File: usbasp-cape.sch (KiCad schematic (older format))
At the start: 1 part

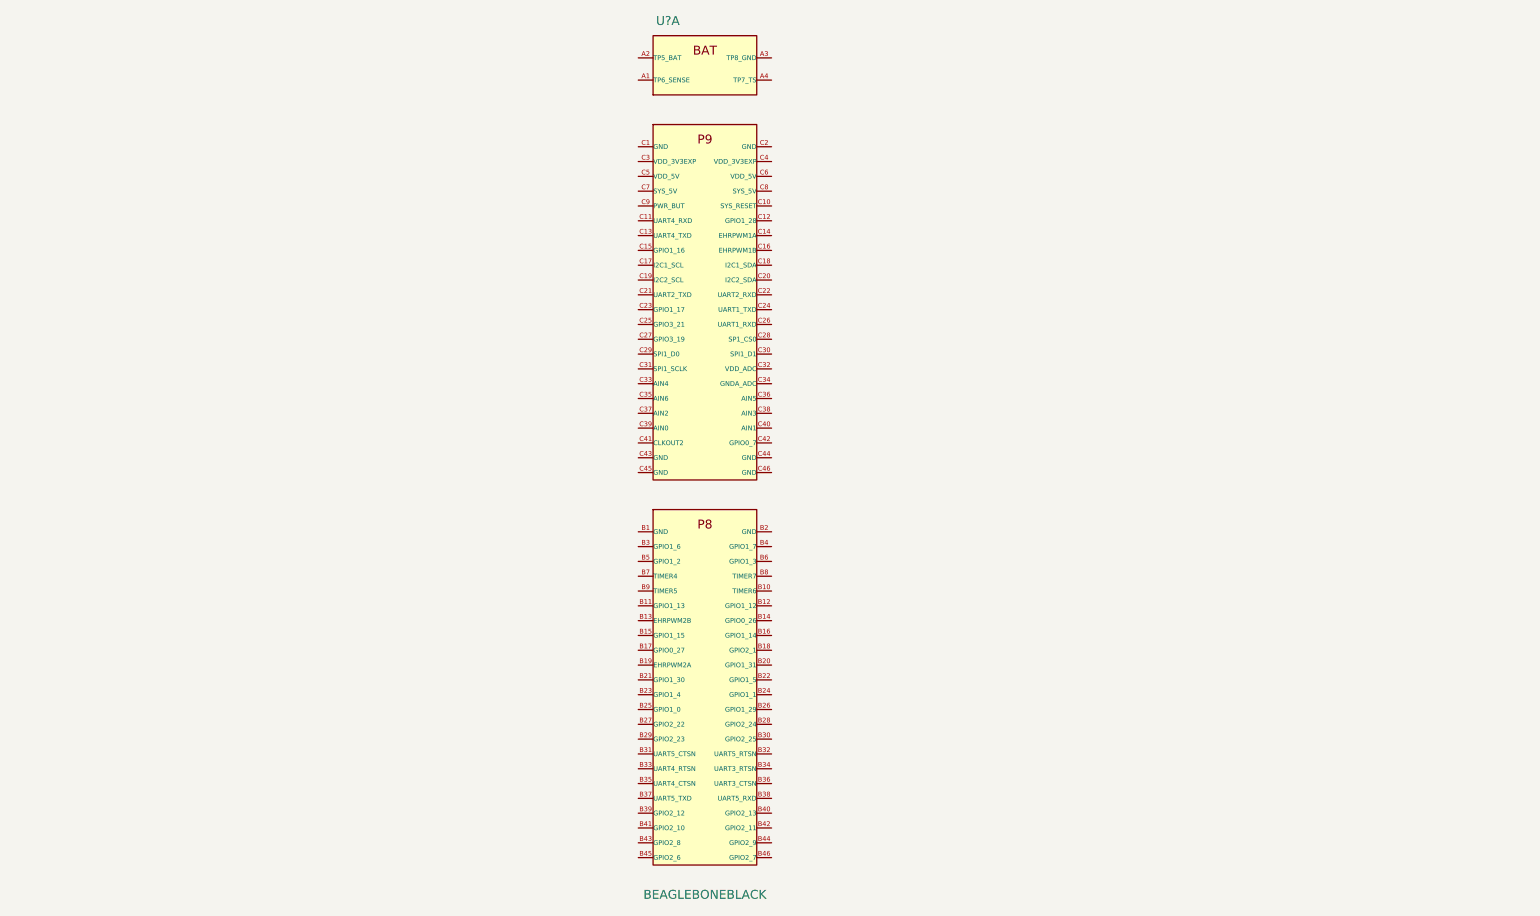
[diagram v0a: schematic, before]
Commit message: add mux and connectors to schematic
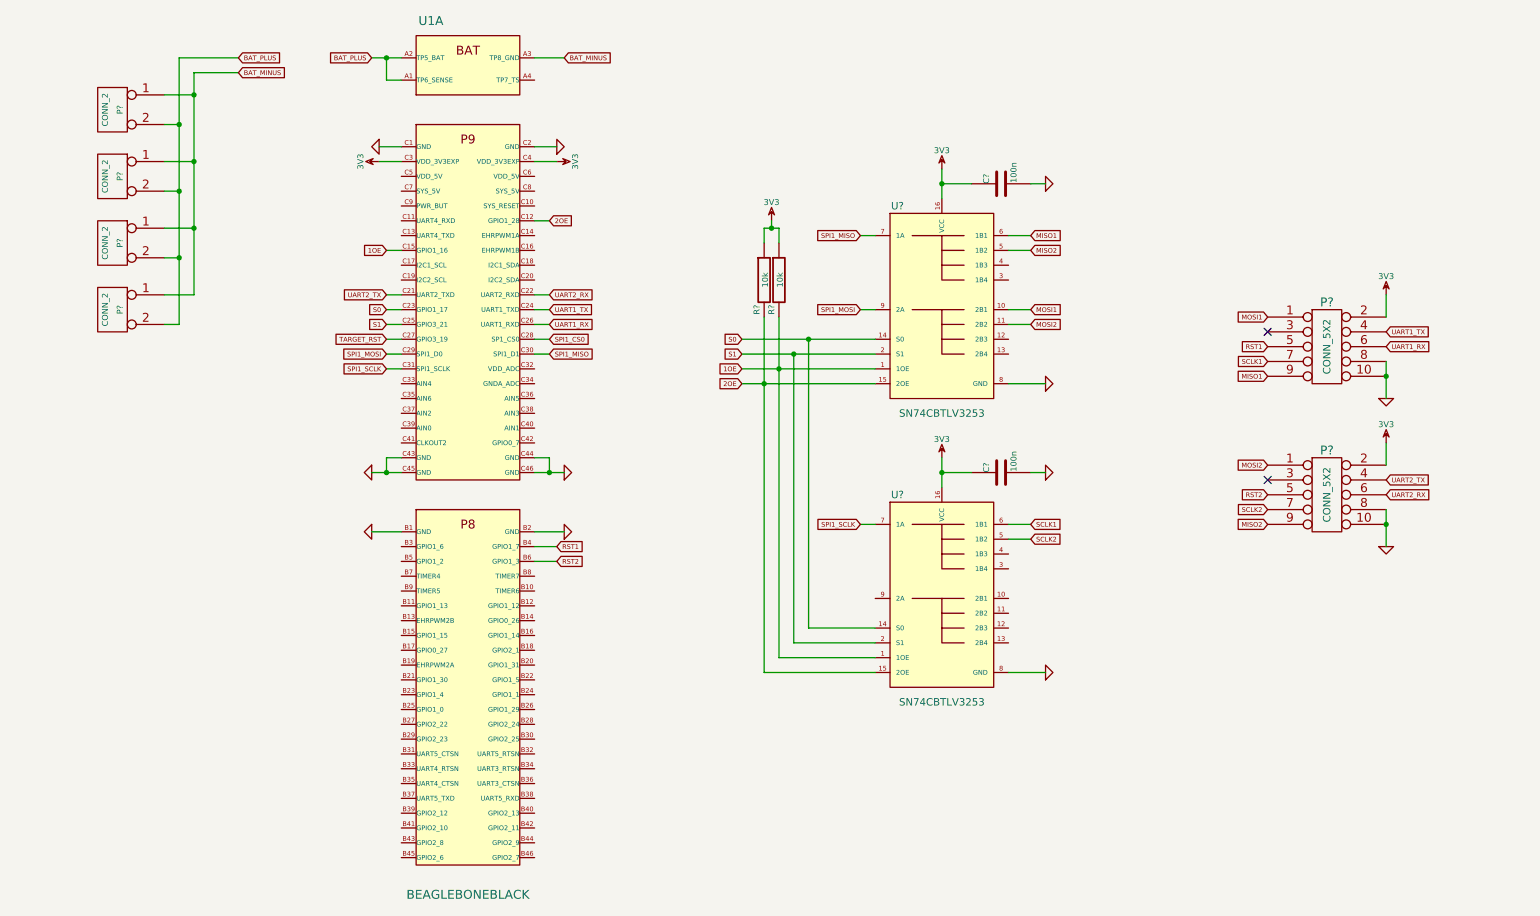
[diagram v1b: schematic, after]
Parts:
- added C? (x2): 100n, symbol C
- added P? (x4): CONN_2, symbol CONN_2
- added P? (x2): CONN_5X2, symbol CONN_5X2
- added R? (x2): 10k, symbol R
- added U? (x2): SN74CBTLV3253, symbol SN74CBTLV3253
- gave numbers to parts that had none: 1
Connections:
- net BAT_PLUS: now reaches U1.A1 (TP6_SENSE)
- net BAT_PLUS: now also U1.A2 (TP5_BAT), P?.2 (PM), P?.2 (PM), P?.2 (PM), P?.2 (PM)
- net BAT_MINUS: now reaches U1.A3 (TP8_GND)
- net BAT_MINUS: now also P?.1 (P1), P?.1 (P1), P?.1 (P1), P?.1 (P1)
- net GND: now reaches U1.B1 (GND)
- net GND: now also U1.B2 (GND), U1.C1 (GND), U1.C2 (GND), U1.C43 (GND), U1.C44 (GND), U1.C45 (GND), U1.C46 (GND), C?.2, C?.2, P?.10, P?.10, P?.8, P?.8, U?.8 (GND), U?.8 (GND)
- net RST1: now reaches U1.B4 (GPIO1_7)
- net RST1: now also P?.5
- net RST2: now reaches U1.B6 (GPIO1_3)
- net RST2: now also P?.5
- net 2OE: now reaches U1.C12 (GPIO1_28)
- net 2OE: now also R?.2, U?.15 (2OE), U?.15 (2OE)
- net 1OE: now reaches U1.C15 (GPIO1_16)
- net 1OE: now also R?.2, U?.1 (1OE), U?.1 (1OE)
- net UART2_TX: now reaches U1.C21 (UART2_TXD)
- net UART2_TX: now also P?.4
- net UART2_RX: now reaches U1.C22 (UART2_RXD)
- net UART2_RX: now also P?.6
- net S0: now reaches U1.C23 (GPIO1_17)
- net S0: now also U?.14 (S0), U?.14 (S0)
- net UART1_TX: now reaches U1.C24 (UART1_TXD)
- net UART1_TX: now also P?.4
- net S1: now reaches U1.C25 (GPIO3_21)
- net S1: now also U?.2 (S1), U?.2 (S1)
- net UART1_RX: now reaches U1.C26 (UART1_RXD)
- net UART1_RX: now also P?.6
- net TARGET_RST: now reaches U1.C27 (GPIO3_19)
- net SPI1_CS0: now reaches U1.C28 (SP1_CS0)
- net SPI1_MOSI: now reaches U1.C29 (SPI1_D0)
- net SPI1_MOSI: now also U?.9 (2A)
- net 3V3: now reaches U1.C3 (VDD_3V3EXP)
- net 3V3: now also U1.C4 (VDD_3V3EXP), C?.1, C?.1, P?.2, P?.2, R?.1, R?.1, U?.16 (VCC), U?.16 (VCC)
- net SPI1_MISO: now reaches U1.C30 (SPI1_D1)
- net SPI1_MISO: now also U?.7 (1A)
- net SPI1_SCLK: now reaches U1.C31 (SPI1_SCLK)
- net SPI1_SCLK: now also U?.7 (1A)
- new net MISO1: P?.9, U?.6 (1B1)
- new net MISO2: P?.9, U?.5 (1B2)
- new net MOSI1: P?.1, U?.10 (2B1)
- new net MOSI2: P?.1, U?.11 (2B2)
- new net SCLK1: P?.7, U?.6 (1B1)
- new net SCLK2: P?.7, U?.5 (1B2)
- no-connect marks 0 -> 2
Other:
- moved on the sheet: U1A

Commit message: add INA219 to schematic
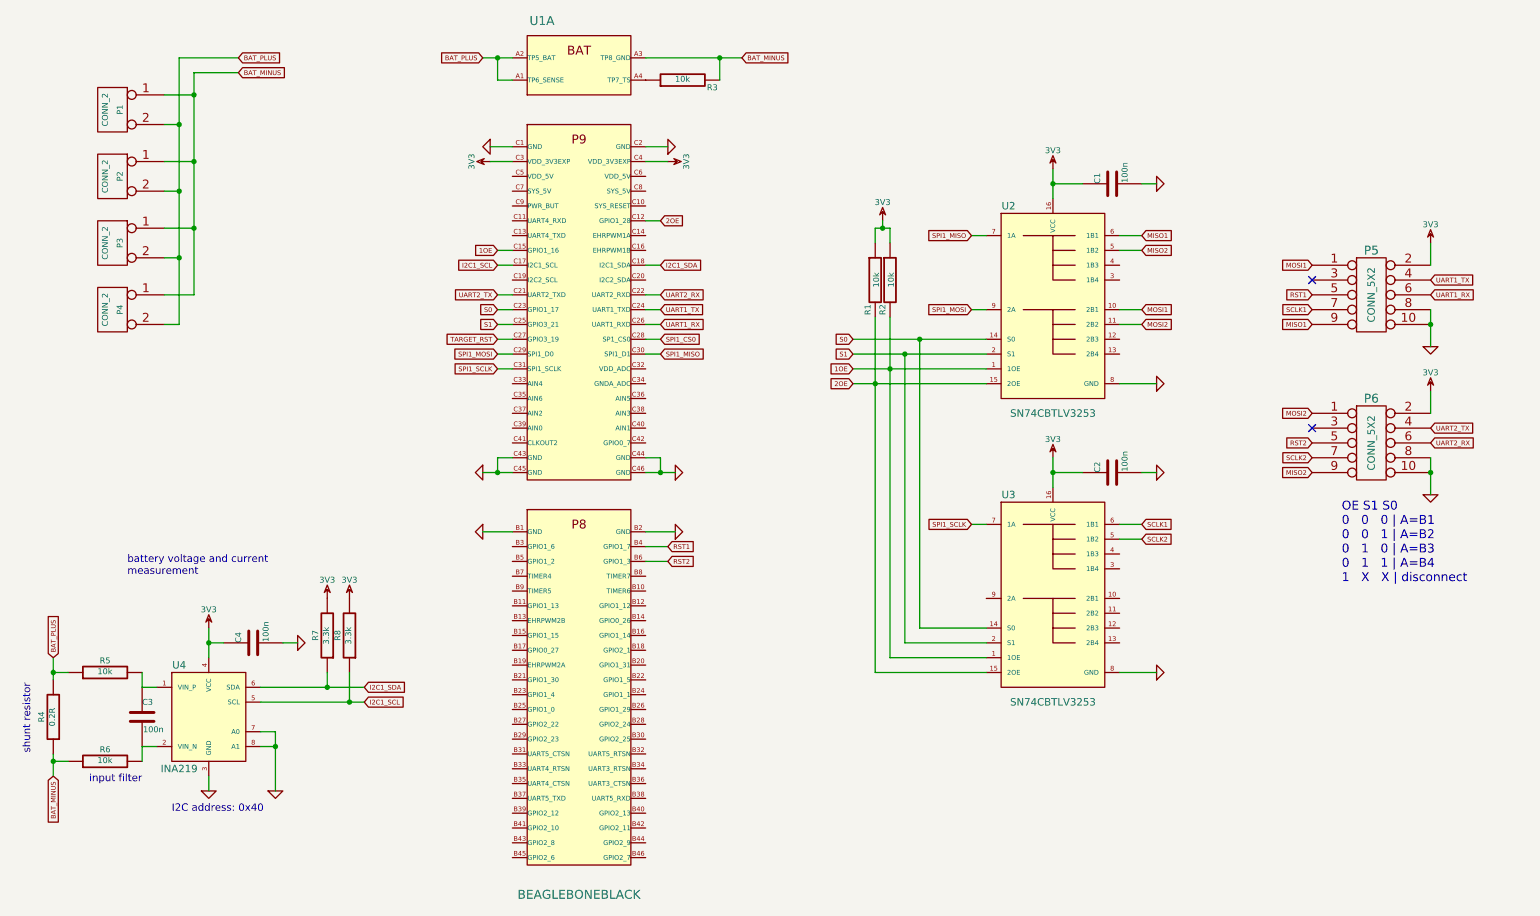
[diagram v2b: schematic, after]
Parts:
- added C3, C4: 100n, symbol C
- added R3, R5, R6: 10k, symbol R
- added R4: 0.2R, symbol R
- added R7, R8: 3.3k, symbol R
- added U4: INA219, symbol INA219
- gave numbers to parts that had none: 12
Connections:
- net 3V3: now also C4.1, R7.2, R8.2, U4.4 (VCC)
- net BAT_MINUS: now also R3.2, R4.1, R6.1
- net BAT_PLUS: now also R4.2, R5.1
- net GND: now also C4.2, U4.3 (GND), U4.7 (A0), U4.8 (A1)
- net at U1.A4 (TP7_TS): now also R3.1
- net I2C1_SCL: now reaches U1.C17 (I2C1_SCL)
- net I2C1_SCL: now also R8.1, U4.5 (SCL)
- net I2C1_SDA: now reaches U1.C18 (I2C1_SDA)
- net I2C1_SDA: now also R7.1, U4.6 (SDA)
- new net: C3.1, R5.2, U4.1 (VIN_P)
- new net: C3.2, R6.2, U4.2 (VIN_N)
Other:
- note added: "I2C address: 0x40"
- note added: "OE S1 S0\n0 0 0 | A=B1\n0 0 1 | A=B2\n0 1 0 | A=B3\n0 1 1 | A=B4\n1 X X | disconnect"
- note added: "battery voltage and current\nmeasurement"
- note added: "input filter"
- note added: "shunt resistor"
- moved on the sheet: C1, C2, P5, P6, R1, R2, U1A, U2, U3

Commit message: rewire some io pins for better routing
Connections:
- net 1OE: now also U1.B15 (GPIO1_15); no longer U1.C15 (GPIO1_16)
- net 2OE: now also U1.B23 (GPIO1_4); no longer U1.C12 (GPIO1_28)
- net BAT_MINUS: no longer R4.1, R6.1
- net BAT_PLUS: no longer U1.A1 (TP6_SENSE), U1.A2 (TP5_BAT)
- net MISO1: now also U2.10 (2B1); no longer U2.6 (1B1)
- net MISO2: now also U2.11 (2B2); no longer U2.5 (1B2)
- net MOSI1: now also U2.6 (1B1); no longer U2.10 (2B1)
- net MOSI2: now also U2.5 (1B2); no longer U2.11 (2B2)
- net RST1: now also U1.C12 (GPIO1_28); no longer U1.B4 (GPIO1_7)
- net RST2: now also U1.B5 (GPIO1_2); no longer U1.B6 (GPIO1_3)
- net S0: now also U1.B25 (GPIO1_0); no longer U1.C23 (GPIO1_17)
- net S1: now also U1.B17 (GPIO0_27); no longer U1.C25 (GPIO3_21)
- net SPI1_MISO: now also U2.9 (2A); no longer U2.7 (1A)
- net SPI1_MOSI: now also U2.7 (1A); no longer U2.9 (2A)
- net UART4_RX: now reaches U1.C11 (UART4_RXD)
- net UART4_RX: now also P6.6
- net UART4_TX: now reaches U1.C13 (UART4_TXD)
- net UART4_TX: now also P6.4
- net UART2_RX: no longer names the net of U1.C22 (UART2_RXD)
- net UART2_RX: no longer P6.6
- net UART2_TX: no longer names the net of U1.C21 (UART2_TXD)
- net UART2_TX: no longer P6.4
- new net BAT_INA_OUT: R4.1, R6.1, U1.A1 (TP6_SENSE), U1.A2 (TP5_BAT)
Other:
- moved on the sheet: C3, C4, P1, P2, P3, P4, R4, R5, R6, R7, R8, U4

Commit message: add BOM
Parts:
- P5, P6: Farnell (none) -> 1022236
- U2, U3: Farnell (none) -> 1752922
- U4: Farnell (none) -> 2295989
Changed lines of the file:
@@
 F 2 "" H 7750 2900 60  0000 C CNN
 F 3 "" H 7750 2900 60  0000 C CNN
+F 4 "1752922" H 7750 2950 60  0001 C CNN "Farnell"
 	1    7750 2950
 	1    0    0    -1
@@
 F 2 "" H 7750 4850 60  0000 C CNN
 F 3 "" H 7750 4850 60  0000 C CNN
+F 4 "1752922" H 7750 4900 60  0001 C CNN "Farnell"
 	1    7750 4900
 	1    0    0    -1
@@
 F 2 "" H 9900 2850 60  0000 C CNN
 F 3 "" H 9900 2850 60  0000 C CNN
+F 4 "1022236" H 9900 2850 60  0001 C CNN "Farnell"
 	1    9900 2850
 	1    0    0    -1
@@
 F 2 "" H 9900 3850 60  0000 C CNN
 F 3 "" H 9900 3850 60  0000 C CNN
+F 4 "1022236" H 9900 3850 60  0001 C CNN "Farnell"
 	1    9900 3850
 	1    0    0    -1
@@
 F 2 "" H 2000 2350 60  0000 C CNN
 F 3 "" H 2000 2350 60  0000 C CNN
+F 4 "2295989" H 2000 2350 60  0001 C CNN "Farnell"
 	1    2000 2350
 	1    0    0    -1
